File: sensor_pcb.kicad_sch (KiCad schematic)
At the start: 35 parts, among them J1 RTDSensor, J3 Conn_01x08, U1 MAX31865, U2 MIC5225, U3 74LVC125

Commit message: Added missing SPN info to parts
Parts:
- J3: SPN (none) -> WM2750-ND; Supplier (none) -> DigiKey
- JP4, JP5, JP6, JP7: SPN (none) -> 732-5316-ND; Supplier (none) -> DigiKey
- U3: SPN (none) -> 296-1222-1-ND; Supplier (none) -> DigiKey
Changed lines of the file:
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@@
 			)
 		)
+		(property "SPN" "296-1222-1-ND"
+			(at 34.29 59.69 0)
+			(effects
+				(font
+					(size 1.27 1.27)
+				)
+				(hide yes)
+			)
+		)
+		(property "Supplier" "DigiKey"
+			(at 34.29 59.69 0)
+			(effects
+				(font
+					(size 1.27 1.27)
+				)
+				(hide yes)
+			)
+		)
 		(pin "1"
 		)
@@
 			)
 		)
+		(property "SPN" "296-1222-1-ND"
+			(at 34.29 78.74 0)
+			(effects
+				(font
+					(size 1.27 1.27)
+				)
+				(hide yes)
+			)
+		)
+		(property "Supplier" "DigiKey"
+			(at 34.29 78.74 0)
+			(effects
+				(font
+					(size 1.27 1.27)
+				)
+				(hide yes)
+			)
+		)
 		(pin "1"
 		)
@@
 			)
 		)
+		(property "SPN" "296-1222-1-ND"
+			(at 64.77 59.69 0)
+			(effects
+				(font
+					(size 1.27 1.27)
+				)
+				(hide yes)
+			)
+		)
+		(property "Supplier" "DigiKey"
+			(at 64.77 59.69 0)
+			(effects
+				(font
+					(size 1.27 1.27)
+				)
+				(hide yes)
+			)
+		)
 		(pin "1"
 		)
@@
 			)
 		)
+		(property "SPN" "296-1222-1-ND"
+			(at 64.77 78.74 0)
+			(effects
+				(font
+					(size 1.27 1.27)
+				)
+				(hide yes)
+			)
+		)
+		(property "Supplier" "DigiKey"
+			(at 64.77 78.74 0)
+			(effects
+				(font
+					(size 1.27 1.27)
+				)
+				(hide yes)
+			)
+		)
 		(pin "1"
 		)
@@
 			)
 		)
+		(property "SPN" "296-1222-1-ND"
+			(at 91.44 69.85 0)
+			(effects
+				(font
+					(size 1.27 1.27)
+				)
+				(hide yes)
+			)
+		)
+		(property "Supplier" "DigiKey"
+			(at 91.44 69.85 0)
+			(effects
+				(font
+					(size 1.27 1.27)
+				)
+				(hide yes)
+			)
+		)
 		(pin "1"
 		)
@@
 			)
 		)
+		(property "SPN" "732-5316-ND"
+			(at 154.94 40.64 0)
+			(effects
+				(font
+					(size 1.27 1.27)
+				)
+				(hide yes)
+			)
+		)
+		(property "Supplier" "DigiKey"
+			(at 154.94 40.64 0)
+			(effects
+				(font
+					(size 1.27 1.27)
+				)
+				(hide yes)
+			)
+		)
 		(pin "3"
 		)
@@
 			)
 		)
+		(property "SPN" "732-5316-ND"
+			(at 154.94 21.59 0)
+			(effects
+				(font
+					(size 1.27 1.27)
+				)
+				(hide yes)
+			)
+		)
+		(property "Supplier" "DigiKey"
+			(at 154.94 21.59 0)
+			(effects
+				(font
+					(size 1.27 1.27)
+				)
+				(hide yes)
+			)
+		)
 		(pin "3"
 		)
@@
 			)
 		)
+		(property "SPN" "732-5316-ND"
+			(at 114.3 40.64 0)
+			(effects
+				(font
+					(size 1.27 1.27)
+				)
+				(hide yes)
+			)
+		)
+		(property "Supplier" "DigiKey"
+			(at 114.3 40.64 0)
+			(effects
+				(font
+					(size 1.27 1.27)
+				)
+				(hide yes)
+			)
+		)
 		(pin "3"
 		)
@@
 			)
 		)
+		(property "SPN" "WM2750-ND"
+			(at 63.5 26.67 0)
+			(effects
+				(font
+					(size 1.27 1.27)
+				)
+				(hide yes)
+			)
+		)
+		(property "Supplier" "DigiKey"
+			(at 63.5 26.67 0)
+			(effects
+				(font
+					(size 1.27 1.27)
+				)
+				(hide yes)
+			)
+		)
 		(pin "8"
 		)
@@
 			(at 114.3 21.59 0)
 			(effects
+				(font
+					(size 1.27 1.27)
+				)
+				(hide yes)
+			)
+		)
+		(property "SPN" "732-5316-ND"
+			(at 114.3 21.59 0)
+			(effects
+				(font
+					(size 1.27 1.27)
+				)
+				(hide yes)
+			)
+		)
+		(property "Supplier" "DigiKey"
+			(at 114.3 21.59 0)
+			(effects

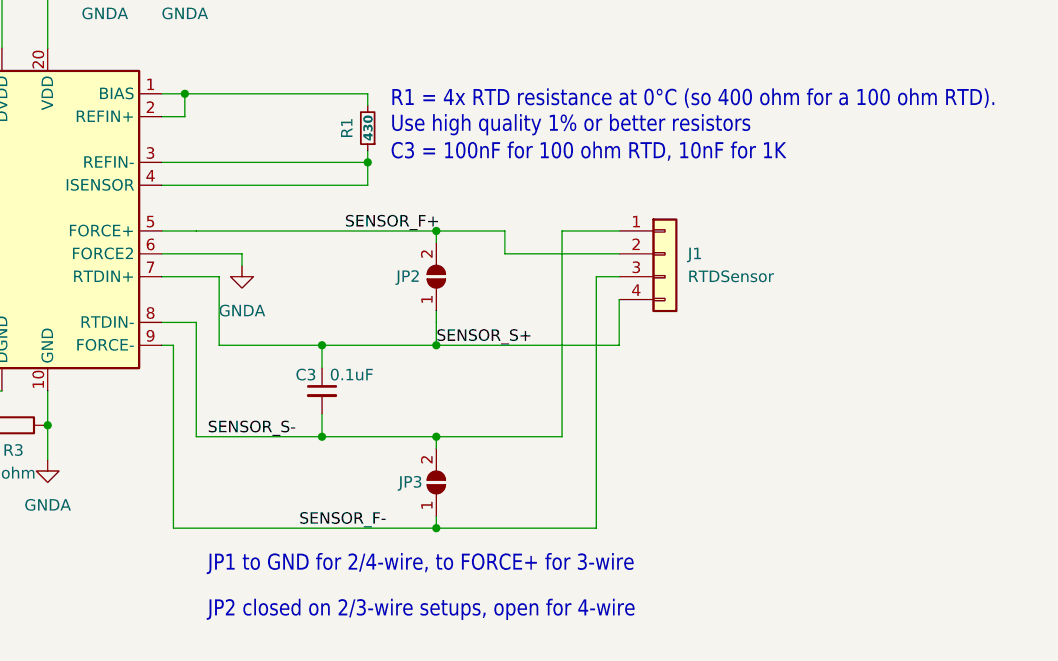
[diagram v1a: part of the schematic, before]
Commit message: RTD sensor wire bonding landing pattern interdigitated
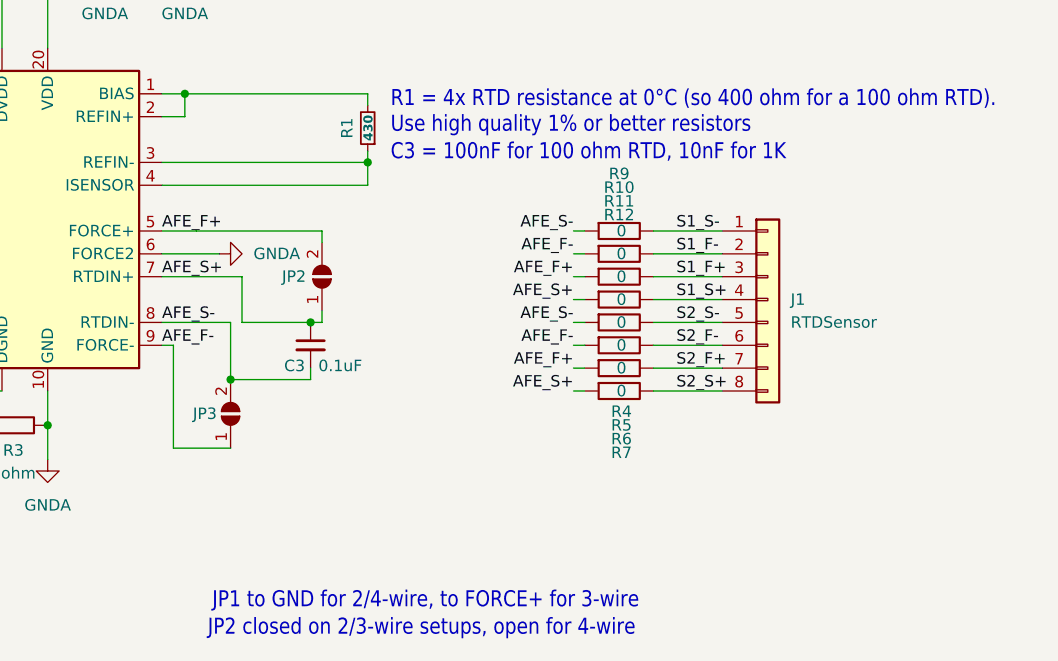
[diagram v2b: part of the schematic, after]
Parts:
- removed J1: RTDSensor, external_footprints:RTD_Sensor_BondPad_4x, symbol Connector_Generic:Conn_01x04
- added J1: RTDSensor, external_footprints:RTD_Sensor_BondPad_interdigitated, symbol Connector_Generic:Conn_01x08
- added R10, R11, R12, R4, R5, R6, R7, R9: 0, Resistor_SMD:R_0805_2012Metric, symbol PCM_SL_Resistors:0ohm
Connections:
- net SENSOR_F+ renamed AFE_F+
- net AFE_F+: now also R11.1, R6.1
- net SENSOR_F- renamed AFE_F-
- net AFE_F-: now also R10.1, R5.1
- net SENSOR_S+ renamed AFE_S+
- net AFE_S+: now also R12.1, R7.1
- net SENSOR_S- renamed AFE_S-
- net AFE_S-: now also R4.1, R9.1
- new net S1_F+: J1.3 (Pin_3), R11.2
- new net S1_F-: J1.2 (Pin_2), R10.2
- new net S1_S+: J1.4 (Pin_4), R12.2
- new net S1_S-: J1.1 (Pin_1), R9.2
- new net S2_F+: J1.7 (Pin_7), R6.2
- new net S2_F-: J1.6 (Pin_6), R5.2
- new net S2_S+: J1.8 (Pin_8), R7.2
- new net S2_S-: J1.5 (Pin_5), R4.2
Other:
- moved on the sheet: C3, JP2, JP3

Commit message: Revision C of layout
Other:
- moved on the sheet: J1, R10, R11, R12, R4, R5, R6, R7, R9
